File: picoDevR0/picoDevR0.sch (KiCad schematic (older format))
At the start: 16 parts, among them J1 Barrel_Jack, J2 Pico1to20, SW1 SW_Push_Dual

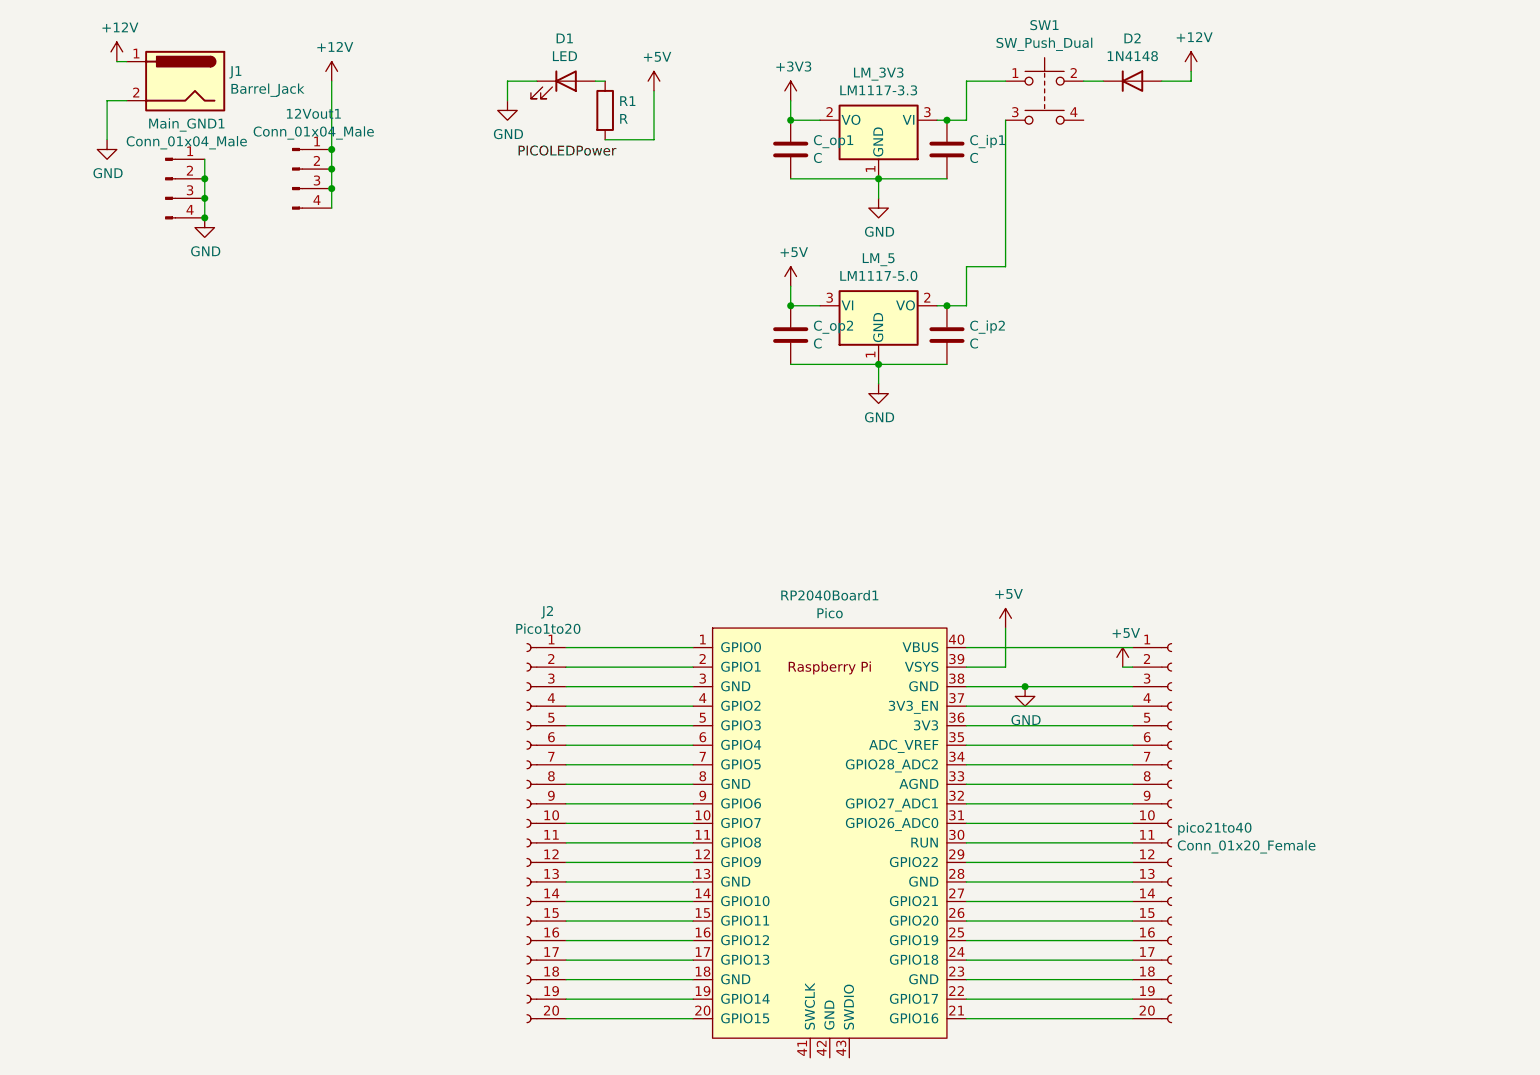
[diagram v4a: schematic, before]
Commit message: reset everything in the PCB
There were many issues with the earlier approach of constantly making changes in the PCB layer after sch like the 5V layer wasn't being accessed by some pins, and so on. Hence it is decided that henceforth the sch will be first finished and then we shall move on to the PCB design part
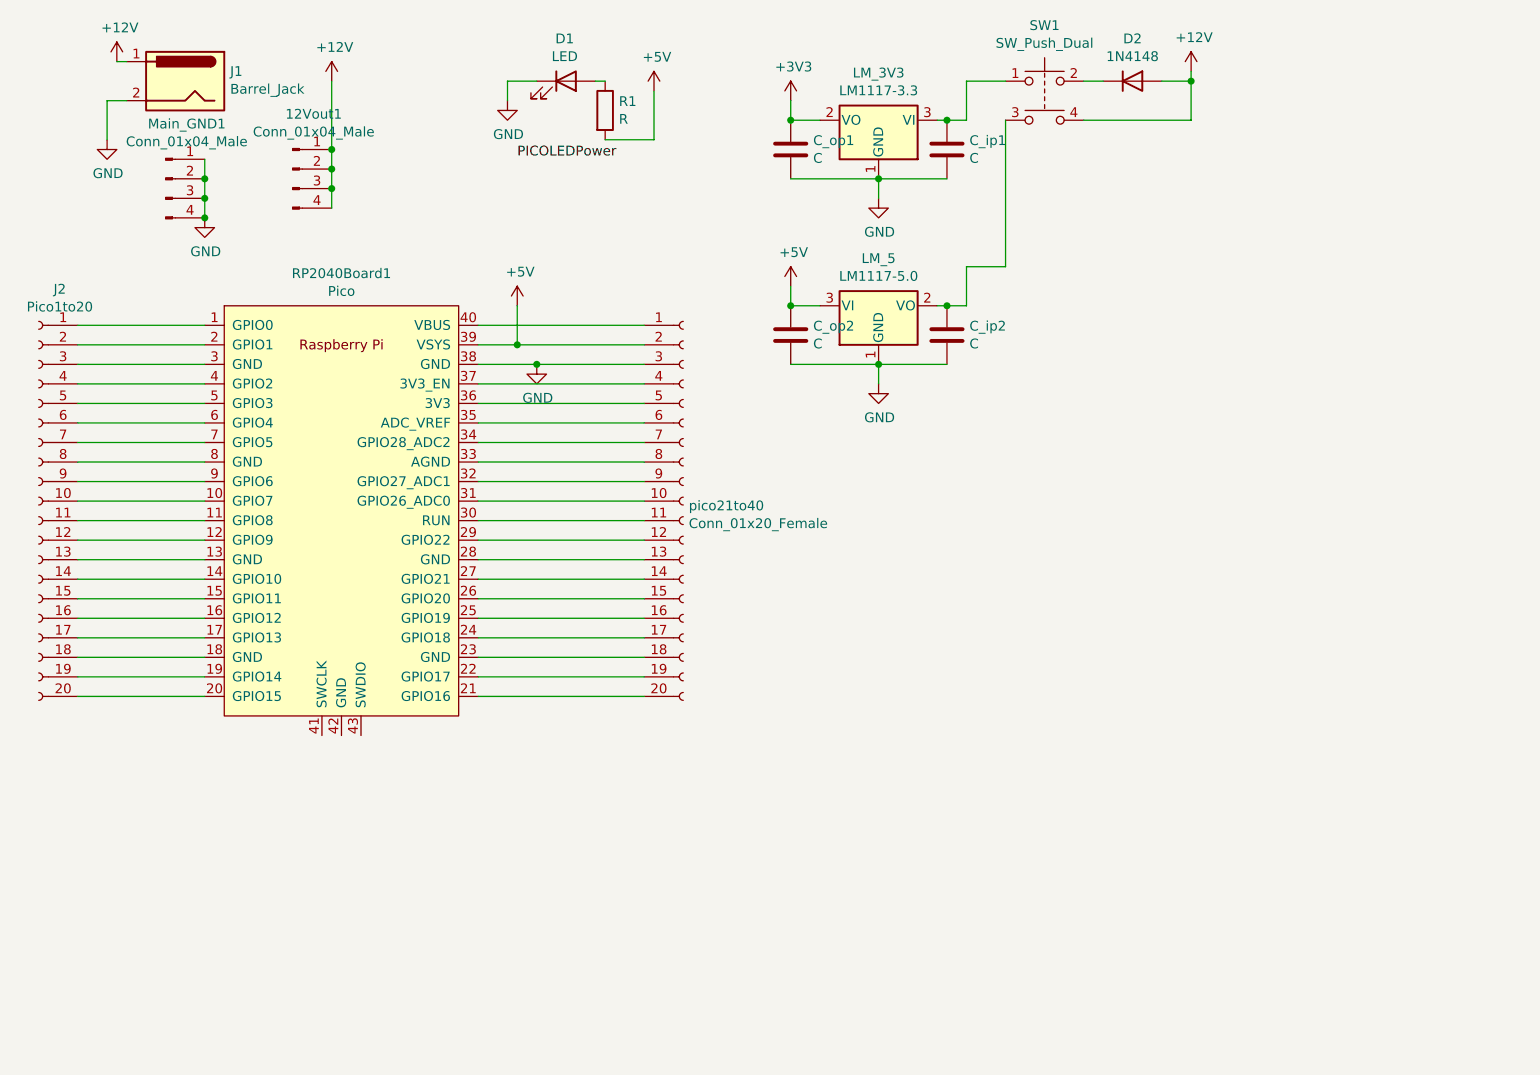
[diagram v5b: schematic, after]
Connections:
- net +12V: now also SW1.4
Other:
- moved on the sheet: J2, RP2040Board1, pico21to40
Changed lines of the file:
@@
 L Connector:Conn_01x20_Female J2
 U 1 1 606F7FA3
-P 3150 4650
-F 0 "J2" H 3042 5735 50  0000 C CNN
-F 1 "Pico1to20" H 3042 5644 50  0000 C CNN
-F 2 "Connector_PinSocket_2.54mm:PinSocket_1x20_P2.54mm_Vertical" H 3150 4650 50  0001 C CNN
-F 3 "~" H 3150 4650 50  0001 C CNN
-	1    3150 4650
+P 650 3000
+F 0 "J2" H 542 4085 50  0000 C CNN
+F 1 "Pico1to20" H 542 3994 50  0000 C CNN
+F 2 "Connector_PinSocket_2.54mm:PinSocket_1x20_P2.54mm_Vertical" H 650 3000 50  0001 C CNN
+F 3 "~" H 650 3000 50  0001 C CNN
+	1    650  3000
 	-1   0    0    -1
 $EndComp
 Wire Wire Line
-	3350 3750 4000 3750
-Wire Wire Line
-	3350 3850 4000 3850
-Wire Wire Line
-	3350 3950 4000 3950
-Wire Wire Line
-	3350 4050 4000 4050
-Wire Wire Line
-	3350 4150 4000 4150
-Wire Wire Line
-	3350 5650 4000 5650
-$Comp
-L Connector:Conn_01x20_Female pico21to40
-U 1 1 606EDD3B
-P 6450 4650
-F 0 "pico21to40" H 6478 4626 50  0000 L CNN
-F 1 "Conn_01x20_Female" H 6478 4535 50  0000 L CNN
-F 2 "Connector_PinSocket_2.54mm:PinSocket_1x20_P2.54mm_Vertical" H 6450 4650 50  0001 C CNN
-F 3 "~" H 6450 4650 50  0001 C CNN
-	1    6450 4650
-	1    0    0    -1
-$EndComp
-Wire Wire Line
-	4000 4250 3350 4250
-Wire Wire Line
-	5400 3750 6250 3750
+	850  2100 1500 2100
+Wire Wire Line
+	850  2200 1500 2200
+Wire Wire Line
+	850  2300 1500 2300
+Wire Wire Line
+	850  2400 1500 2400
+Wire Wire Line
+	850  2500 1500 2500
+Wire Wire Line
+	850  4000 1500 4000
+Wire Wire Line
+	1500 2600 850  2600
+Wire Wire Line
+	2900 2100 3750 2100
 $Comp
 L picoLibRP2040:Pico RP2040Board1
 U 1 1 60A03192
-P 4700 4700
-F 0 "RP2040Board1" H 4700 5915 50  0000 C CNN
-F 1 "Pico" H 4700 5824 50  0000 C CNN
-F 2 "picoFootPrint:RPi_Pico_SMD_TH" V 4700 4700 50  0001 C CNN
-F 3 "" H 4700 4700 50  0001 C CNN
-	1    4700 4700
-	1    0    0    -1
-$EndComp
-Wire Wire Line
-	5400 5650 6250 5650
+P 2200 3050
+F 0 "RP2040Board1" H 2200 4265 50  0000 C CNN
+F 1 "Pico" H 2200 4174 50  0000 C CNN
+F 2 "picoFootPrint:RPi_Pico_SMD_TH" V 2200 3050 50  0001 C CNN
+F 3 "" H 2200 3050 50  0001 C CNN
+	1    2200 3050
+	1    0    0    -1
+$EndComp
+Wire Wire Line
+	2900 4000 3750 4000
 $Comp
 L Regulator_Linear:LM1117-3.3 LM_3V3
@@
 	4950 1350 5300 1350
 Wire Wire Line
-	5400 4050 6250 4050
-Wire Wire Line
-	5400 4150 6250 4150
-Wire Wire Line
-	6250 4250 5400 4250
-Wire Wire Line
-	6250 4350 5400 4350
-Wire Wire Line
-	5400 4450 6250 4450
-Wire Wire Line
-	6250 4550 5400 4550
-Wire Wire Line
-	6250 4650 5400 4650
-Wire Wire Line
-	6250 4750 5400 4750
-Wire Wire Line
-	6250 4850 5400 4850
-Wire Wire Line
-	5400 4950 6250 4950
-Wire Wire Line
-	6250 5050 5400 5050
-Wire Wire Line
-	5400 5150 6250 5150
-Wire Wire Line
-	5400 5250 6250 5250
-Wire Wire Line
-	5400 5350 6250 5350
-Wire Wire Line
-	5400 5450 6250 5450
-Wire Wire Line
-	6250 5550 5400 5550
-Wire Wire Line
-	4000 4350 3350 4350
-Wire Wire Line
-	4000 4450 3350 4450
-Wire Wire Line
-	4000 4550 3350 4550
-Wire Wire Line
-	4000 4650 3350 4650
-Wire Wire Line
-	3350 4750 4000 4750
-Wire Wire Line
-	3350 4850 4000 4850
-Wire Wire Line
-	4000 4950 3350 4950
-Wire Wire Line
-	3350 5050 4000 5050
-Wire Wire Line
-	4000 5150 3350 5150
-Wire Wire Line
-	3350 5250 4000 5250
-Wire Wire Line
-	4000 5350 3350 5350
-Wire Wire Line
-	3350 5450 4000 5450
-Wire Wire Line
-	4000 5550 3350 5550
+	2900 2400 3750 2400
+Wire Wire Line
+	2900 2500 3750 2500
+Wire Wire Line
+	3750 2600 2900 2600
+Wire Wire Line
+	3750 2700 2900 2700
+Wire Wire Line
+	2900 2800 3750 2800
+Wire Wire Line
+	3750 2900 2900 2900
+Wire Wire Line
+	3750 3000 2900 3000
+Wire Wire Line
+	3750 3100 2900 3100
+Wire Wire Line
+	3750 3200 2900 3200
+Wire Wire Line
+	2900 3300 3750 3300
+Wire Wire Line
+	3750 3400 2900 3400
+Wire Wire Line
+	2900 3500 3750 3500
+Wire Wire Line
+	2900 3600 3750 3600
+Wire Wire Line
+	2900 3700 3750 3700
+Wire Wire Line
+	2900 3800 3750 3800
+Wire Wire Line
+	3750 3900 2900 3900
+Wire Wire Line
+	1500 2700 850  2700
+Wire Wire Line
+	1500 2800 850  2800
+Wire Wire Line
+	1500 2900 850  2900
+Wire Wire Line
+	1500 3000 850  3000
+Wire Wire Line
+	850  3100 1500 3100
+Wire Wire Line
+	850  3200 1500 3200
+Wire Wire Line
+	1500 3300 850  3300
+Wire Wire Line
+	850  3400 1500 3400
+Wire Wire Line
+	1500 3500 850  3500
+Wire Wire Line
+	850  3600 1500 3600
+Wire Wire Line
+	1500 3700 850  3700
+Wire Wire Line
+	850  3800 1500 3800
+Wire Wire Line
+	1500 3900 850  3900
 $Comp
 L Device:R R1
@@
 	4500 1050 4500 950
 Wire Wire Line
-	6250 3950 5700 3950
+	3750 2300 3200 2300
 $Comp
 L power:GND #PWR0105
 U 1 1 60A453D2
-P 5700 3950
-F 0 "#PWR0105" H 5700 3700 50  0001 C CNN
-F 1 "GND" H 5705 3777 50  0000 C CNN
-F 2 "" H 5700 3950 50  0001 C CNN
-F 3 "" H 5700 3950 50  0001 C CNN
-	1    5700 3950
-	1    0    0    -1
-$EndComp
-Connection ~ 5700 3950
-Wire Wire Line
-	5700 3950 5400 3950
+P 3200 2300
+F 0 "#PWR0105" H 3200 2050 50  0001 C CNN
+F 1 "GND" H 3205 2127 50  0000 C CNN
+F 2 "" H 3200 2300 50  0001 C CNN
+F 3 "" H 3200 2300 50  0001 C CNN
+	1    3200 2300
+	1    0    0    -1
+$EndComp
+Connection ~ 3200 2300
+Wire Wire Line
+	3200 2300 2900 2300
 $Comp
 L Device:C C_op1
@@
 $EndComp
 Wire Wire Line
-	5600 3650 5600 3850
+	3100 2000 3100 2200
 $Comp
 L power:+5V #PWR0104
@@
 L power:+5V #PWR0106
 U 1 1 60C79A6B
-P 5600 3650
-F 0 "#PWR0106" H 5600 3500 50  0001 C CNN
-F 1 "+5V" H 5615 3823 50  0000 C CNN
-F 2 "" H 5600 3650 50  0001 C CNN
-F 3 "" H 5600 3650 50  0001 C CNN
-	1    5600 3650
+P 3100 2000
+F 0 "#PWR0106" H 3100 1850 50  0001 C CNN
+F 1 "+5V" H 3115 2173 50  0000 C CNN
+F 2 "" H 3100 2000 50  0001 C CNN
+F 3 "" H 3100 2000 50  0001 C CNN
+	1    3100 2000
 	1    0    0    -1
 $EndComp
@@
 	3800 1150 3800 900
 Wire Wire Line
-	5400 3850 5600 3850
+	2900 2200 3100 2200
 $Comp
 L Diode:1N4148 D2
@@
 	1    0    0    -1
 $EndComp
-$Comp
-L power:+5V #PWR0114
-U 1 1 60CB5175
-P 6200 3850
-F 0 "#PWR0114" H 6200 3700 50  0001 C CNN
-F 1 "+5V" H 6215 4023 50  0000 C CNN
-F 2 "" H 6200 3850 50  0001 C CNN
-F 3 "" H 6200 3850 50  0001 C CNN
-	1    6200 3850
-	1    0    0    -1
-$EndComp
-Wire Wire Line
-	6250 3850 6200 3850
+Wire Wire Line
+	6000 1050 6550 1050
+Wire Wire Line
+	6550 1050 6550 850
+Connection ~ 6550 850
+$Comp
+L Connector:Conn_01x20_Female pico21to40
+U 1 1 606EDD3B
+P 3950 3000
+F 0 "pico21to40" H 3978 2976 50  0000 L CNN
+F 1 "Conn_01x20_Female" H 3978 2885 50  0000 L CNN
+F 2 "Connector_PinSocket_2.54mm:PinSocket_1x20_P2.54mm_Vertical" H 3950 3000 50  0001 C CNN
+F 3 "~" H 3950 3000 50  0001 C CNN
+	1    3950 3000
+	1    0    0    -1
+$EndComp
+Wire Wire Line
+	3100 2200 3750 2200
+Connection ~ 3100 2200
 $EndSCHEMATC
